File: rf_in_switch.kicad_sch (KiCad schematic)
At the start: 7 parts, among them P17 CONUFL001-SMD-T, P18 CONUFL001-SMD-T, U31 QPC1022TR7, U32 QPC1022TR7

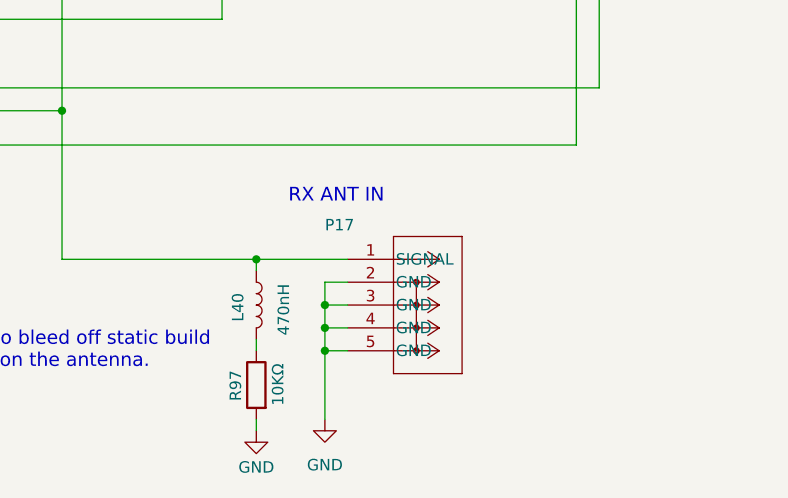
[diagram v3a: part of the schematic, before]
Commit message: Clean up the U.FL connectors a little more
Re-add the ones for TX/RX so both MMCX and U.FL are available.

Move P8 to a better location.

Signed-off-by: Corey Minyard <corey@minyard.net>
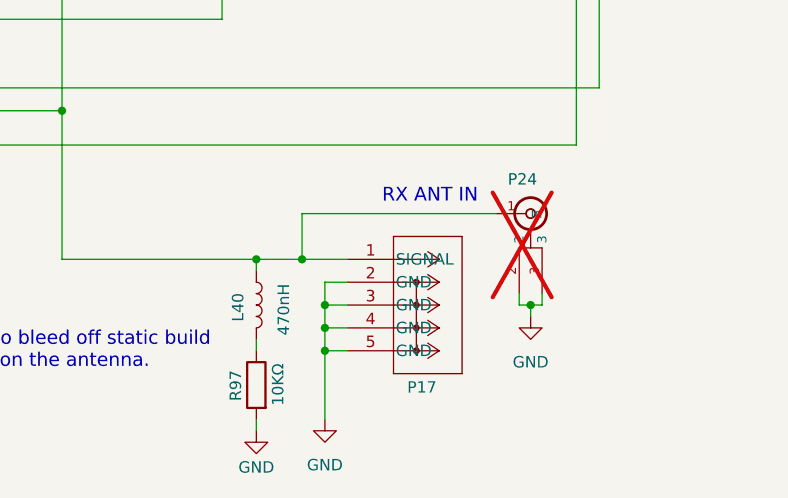
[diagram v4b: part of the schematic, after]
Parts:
- added P24: CONUFL001-SMD-T, PacSatDev_misc:CONN1_CONUFL_TEC, symbol PACSAT_DEV_misc:U_FL
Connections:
- net GND: now also P24.2, P24.3
- net at L40.1, P17.1 (SIGNAL), R96.1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: now also P24.1 (In)
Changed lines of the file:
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@@
 	(text "RX ANT IN"
 		(exclude_from_sim no)
-		(at 157.734 141.224 0)
+		(at 168.148 141.224 0)
 		(effects
 			(font
@@
 	)
 	(junction
+		(at 148.59 147.32)
+		(diameter 0)
+		(color 0 0 0 0)
+	)
+	(junction
 		(at 139.7 113.03)
 		(diameter 0)
@@
 	)
 	(junction
+		(at 173.99 152.4)
+		(diameter 0)
+		(color 0 0 0 0)
+	)
+	(junction
 		(at 151.13 157.48)
 		(diameter 0)
@@
 	(wire
 		(pts
+			(xy 172.72 151.13) (xy 172.72 152.4)
+		)
+		(stroke
+			(width 0)
+			(type default)
+		)
+	)
+	(wire
+		(pts
 			(xy 181.61 109.22) (xy 181.61 128.27)
 		)
@@
 	(wire
 		(pts
+			(xy 148.59 147.32) (xy 153.67 147.32)
+		)
+		(stroke
+			(width 0)
+			(type default)
+		)
+	)
+	(wire
+		(pts
 			(xy 121.92 147.32) (xy 121.92 130.81)
 		)
@@
 	(wire
 		(pts
+			(xy 173.99 152.4) (xy 172.72 152.4)
+		)
+		(stroke
+			(width 0)
+			(type default)
+		)
+	)
+	(wire
+		(pts
 			(xy 104.14 74.93) (xy 109.22 74.93)
 		)
@@
 	(wire
 		(pts
-			(xy 143.51 147.32) (xy 153.67 147.32)
+			(xy 175.26 152.4) (xy 173.99 152.4)
+		)
+		(stroke
+			(width 0)
+			(type default)
+		)
+	)
+	(wire
+		(pts
+			(xy 143.51 147.32) (xy 148.59 147.32)
 		)
 		(stroke
@@
 	(wire
 		(pts
+			(xy 148.59 142.24) (xy 148.59 147.32)
+		)
+		(stroke
+			(width 0)
+			(type default)
+		)
+	)
+	(wire
+		(pts
 			(xy 106.68 53.34) (xy 106.68 68.58)
 		)
@@
 	(wire
 		(pts
+			(xy 173.99 153.67) (xy 173.99 152.4)
+		)
+		(stroke
+			(width 0)
+			(type default)
+		)
+	)
+	(wire
+		(pts
 			(xy 198.12 64.77) (xy 198.12 82.55)
 		)
@@
 	(wire
 		(pts
+			(xy 170.18 142.24) (xy 148.59 142.24)
+		)
+		(stroke
+			(width 0)
+			(type default)
+		)
+	)
+	(wire
+		(pts
 			(xy 163.83 55.88) (xy 163.83 58.42)
 		)
@@
 		(pts
 			(xy 101.6 77.47) (xy 118.11 77.47)
+		)
+		(stroke
+			(width 0)
+			(type default)
+		)
+	)
+	(wire
+		(pts
+			(xy 175.26 151.13) (xy 175.26 152.4)
 		)
 		(stroke
@@
 	)
 	(symbol
+		(lib_id "power:GND")
+		(at 173.99 153.67 0)
+		(mirror y)
+		(unit 1)
+		(exclude_from_sim no)
+		(in_bom yes)
+		(on_board yes)
+		(dnp no)
+		(fields_autoplaced yes)
+		(property "Reference" "#PWR0253"
+			(at 173.99 160.02 0)
+			(effects
+				(font
+					(size 1.27 1.27)
+				)
+				(hide yes)
+			)
+		)
+		(property "Value" "GND"
+			(at 173.99 158.75 0)
+			(effects
+				(font
+					(size 1.27 1.27)
+				)
+			)
+		)
+		(property "Footprint" ""
+			(at 173.99 153.67 0)
+			(effects
+				(font
+					(size 1.27 1.27)
+				)
+				(hide yes)
+			)
+		)
+		(property "Datasheet" ""
+			(at 173.99 153.67 0)
+			(effects
+				(font
+					(size 1.27 1.27)
+				)
+				(hide yes)
+			)
+		)
+		(property "Description" ""
+			(at 173.99 153.67 0)
+			(effects
+				(font
+					(size 1.27 1.27)
+				)
+			)
+		)
+		(pin "1"
+		)
+		(instances
+			(project "PacSat_AFSK"
+				(path "/cc9f42d2-6985-41ac-acab-5ab7b01c5b38/4fa888af-703c-49ed-93bb-d56d2f02c470/64a91b23-a882-4658-bea9-c6c8274e2ac4"
+					(reference "#PWR0253")
+					(unit 1)
+				)
+			)
+		)
+	)
+	(symbol
 		(lib_id "power:+5V")
 		(at 83.82 118.11 0)
@@
 				(path "/cc9f42d2-6985-41ac-acab-5ab7b01c5b38/4fa888af-703c-49ed-93bb-d56d2f02c470/64a91b23-a882-4658-bea9-c6c8274e2ac4"
 					(reference "#PWR0275")
+					(unit 1)
+				)
+			)
+		)
+	)
+	(symbol
+		(lib_id "PACSAT_DEV_misc:U_FL")
+		(at 173.99 142.24 0)
+		(unit 1)
+		(exclude_from_sim no)
+		(in_bom no)
+		(on_board yes)
+		(dnp yes)
+		(property "Reference" "P24"
+			(at 171.45 138.43 0)
+			(effects
+				(font
+					(size 1.27 1.27)
+				)
+				(justify left)
+			)
+		)
+		(property "Value" "CONUFL001-SMD-T"
+			(at 173.99 142.24 0)
+			(effects
+				(font
+					(size 1.27 1.27)
+				)
+				(hide yes)
+			)
+		)
+		(property "Footprint" "PacSatDev_misc:CONN1_CONUFL_TEC"
+			(at 173.99 142.24 0)
+			(effects
+				(font
+					(size 1.27 1.27)
+				)
+				(hide yes)
+			)
+		)
+		(property "Datasheet" ""
+			(at 173.99 142.24 0)
+			(effects
+				(font
+					(size 1.27 1.27)
+				)
+				(hide yes)
+			)
+		)
+		(property "Description" ""
+			(at 173.99 142.24 0)
+			(effects
+				(font
+					(size 1.27 1.27)
+				)
+			)
+		)
+		(pin "1"
+		)
+		(pin "2"
+		)
+		(pin "3"
+		)
+		(instances
+			(project "PacSat_AFSK"
+				(path "/cc9f42d2-6985-41ac-acab-5ab7b01c5b38/4fa888af-703c-49ed-93bb-d56d2f02c470/64a91b23-a882-4658-bea9-c6c8274e2ac4"
+					(reference "P24")
 					(unit 1)
 				)
@@
 		(dnp no)
 		(property "Reference" "P17"
-			(at 151.13 143.51 0)
-			(effects
-				(font
+			(at 160.274 161.544 0)
+			(effects
+				(font

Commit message: Set the part number right for the MMCX connectors
Signed-off-by: Corey Minyard <corey@minyard.net>
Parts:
- P17: value CONUFL001-SMD-T -> MMCX-J-P-H-ST-TH1
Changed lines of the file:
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@@
 			)
 		)
-		(property "Value" "CONUFL001-SMD-T"
+		(property "Value" "MMCX-J-P-H-ST-TH1"
 			(at 153.67 147.32 0)
 			(effects

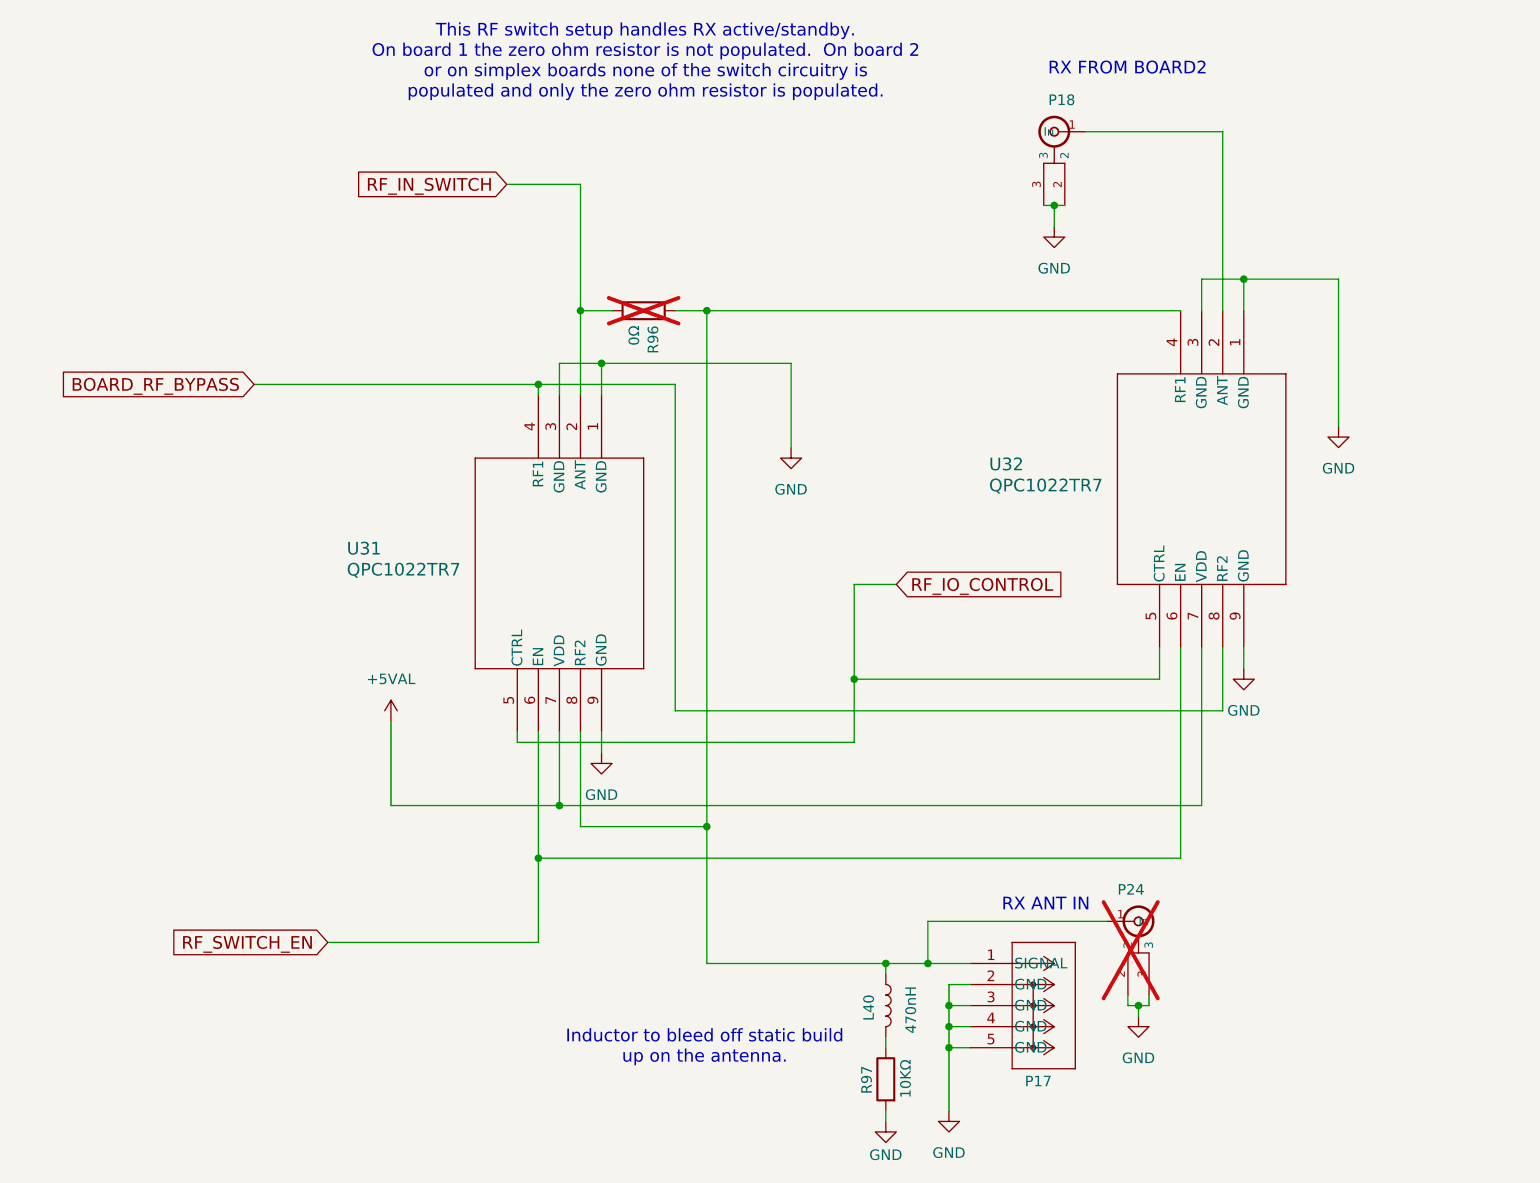
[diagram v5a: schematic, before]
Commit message: Rework RF switches, remove loopback
The loopback just wasn't going to work.  Use a different, more suitable
RF switch.  This required adding a new power converter for 3.3VAL.

Move the power limiters to their own sheet to make things a little more
roomy on the power sheet.

Signed-off-by: Corey Minyard <corey@minyard.net>
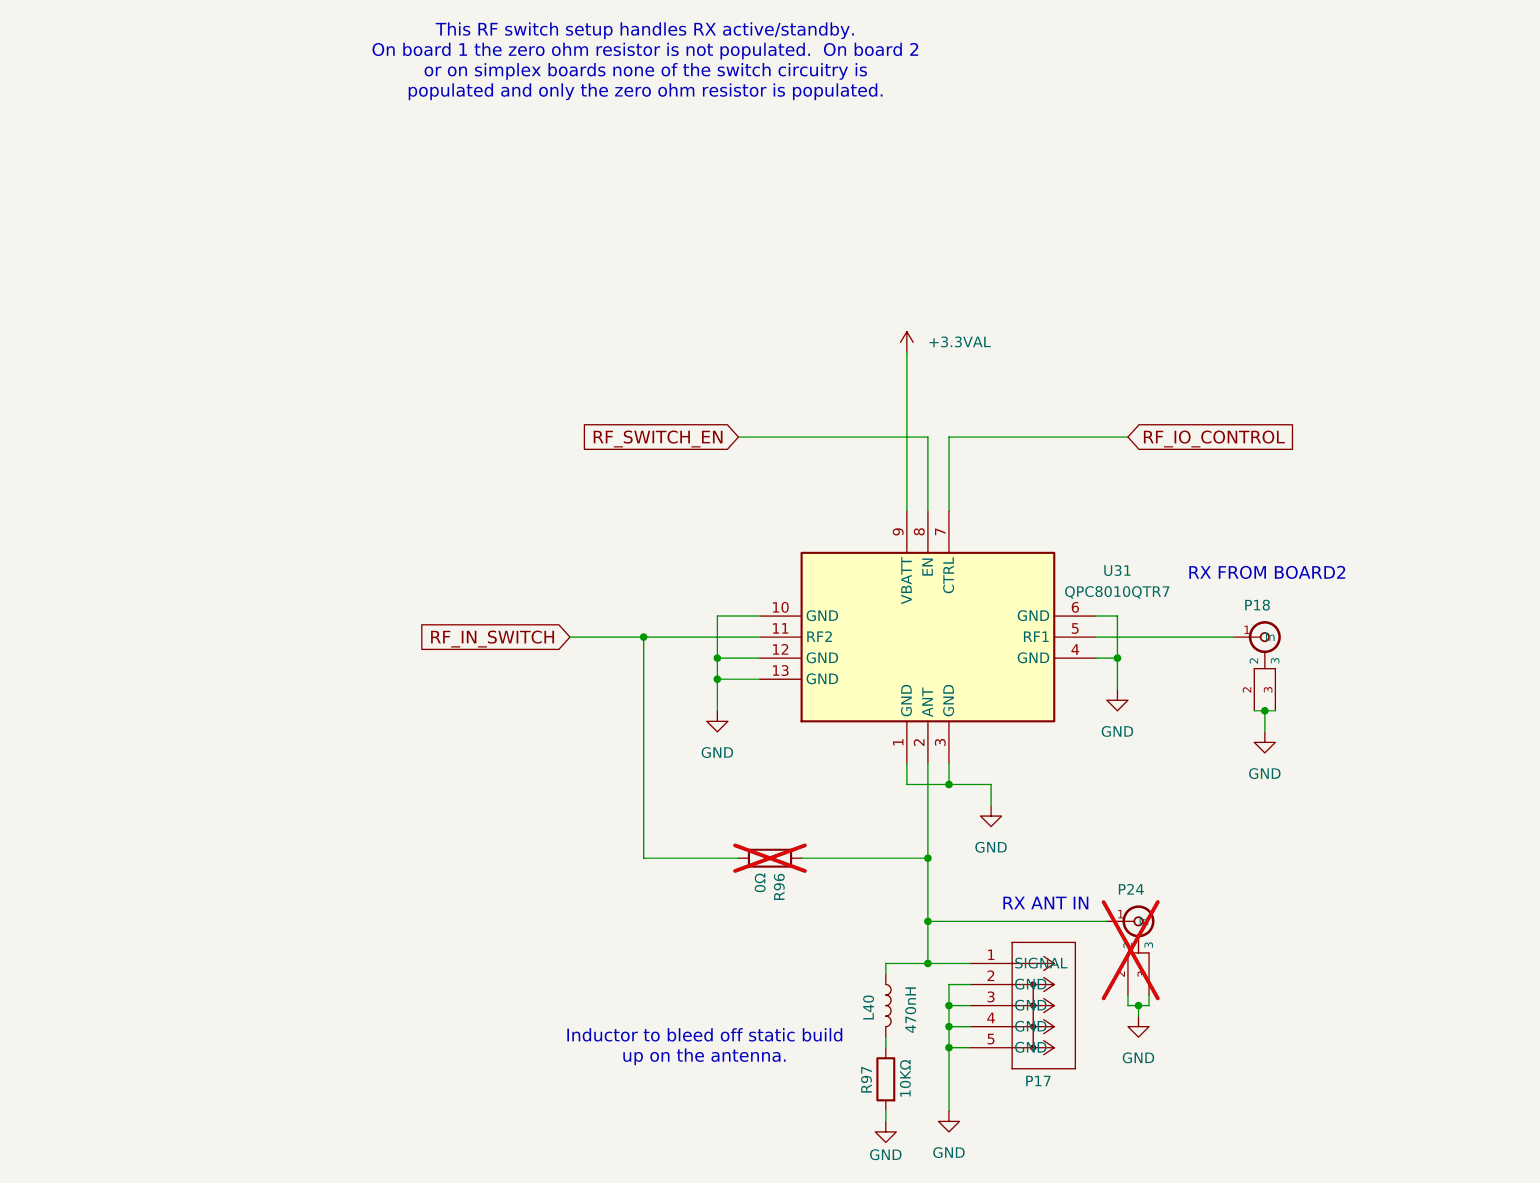
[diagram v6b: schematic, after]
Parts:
- removed U31, U32: QPC1022TR7, PacSatDev_misc:QPC1022_QOR, symbol PACSAT_DEV_misc:QPC1022TR7
- added U31: QPC8010QTR7, PacSatDev_misc:QFN50P200X200X60-13N-D, symbol PACSAT_DEV_misc:QPC8010QTR7
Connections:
- net GND: now also U31.1 (GND), U31.10 (GND), U31.12 (GND), U31.13 (GND), U31.3 (GND), U31.4 (GND), U31.6 (GND)
- net RF_IN_SWITCH: now also U31.11 (RF2)
- net RF_IO_CONTROL: now also U31.7 (CTRL)
- net RF_SWITCH_EN: now also U31.8 (EN)
- net at L40.1, P17.1 (SIGNAL), P24.1 (In)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: now also U31.2 (ANT)
- net at P18.1 (In): now also U31.5 (RF1)
- new net +3.3VAL: U31.9 (VBATT)
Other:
- moved on the sheet: P18, R96

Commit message: Fixes for the RF switch changes
The RF outputs were backwards and needed to be switched.  That required
flipping the chips to the top and the bypass resistors to the bottom.

Fix various documentation around the new parts and the loss of the
loopback function.

Signed-off-by: Corey Minyard <corey@minyard.net>
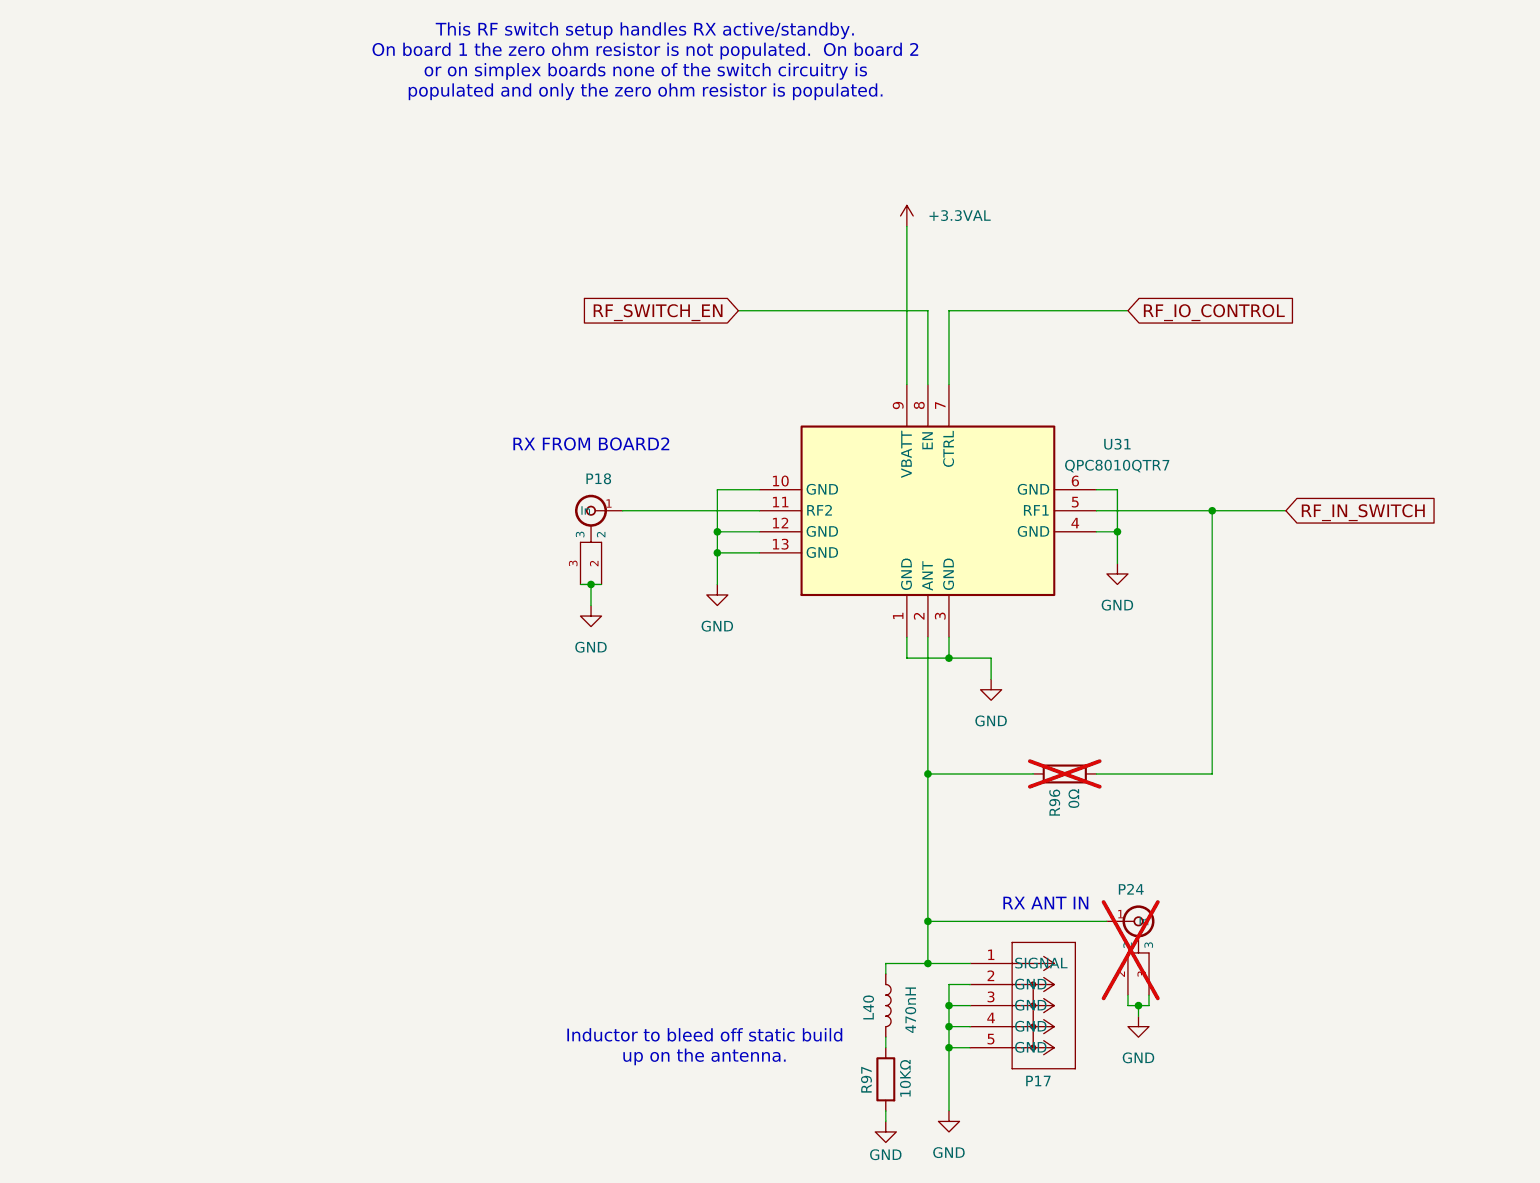
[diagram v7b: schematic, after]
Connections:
- net RF_IN_SWITCH: now also U31.5 (RF1); no longer U31.11 (RF2)
- net at P18.1 (In): now also U31.11 (RF2); no longer U31.5 (RF1)
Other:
- moved on the sheet: P18, R96, U31

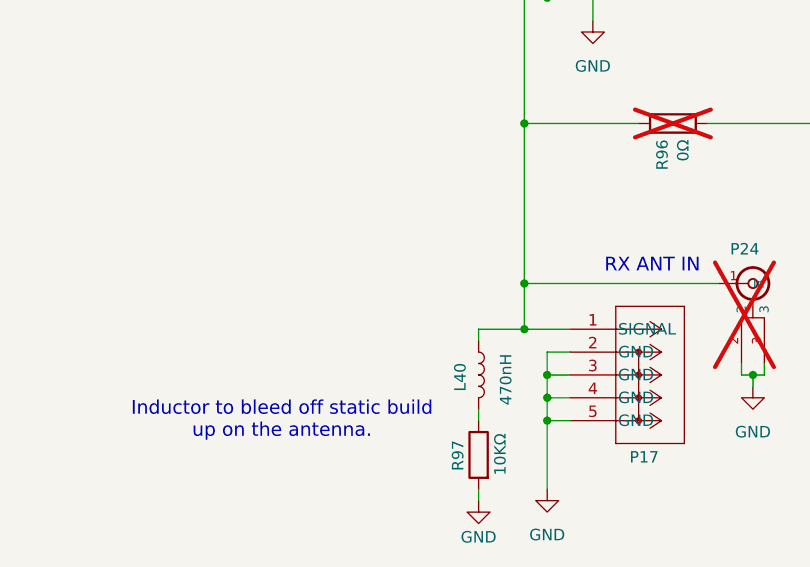
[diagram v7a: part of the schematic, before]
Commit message: Add an optional diplexed antenna input
Signed-off-by: Corey Minyard <corey@minyard.net>
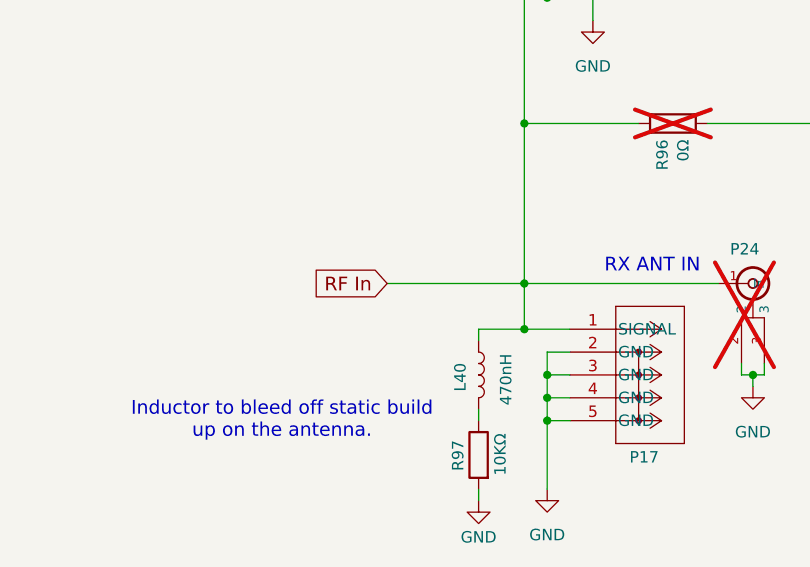
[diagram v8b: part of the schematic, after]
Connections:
- net RF In: now reaches L40.1, P17.1 (SIGNAL), P24.1 (In), R96.1, U31.2 (ANT)
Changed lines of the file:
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@@
+	(wire
+		(pts
+			(xy 133.35 142.24) (xy 148.59 142.24)
+		)
+		(stroke
+			(width 0)
+			(type default)
+		)
+	)
 	(wire
 		(pts
@@
 				(hide yes)
 			)
+		)
+	)
+	(global_label "RF In"
+		(shape input)
+		(at 133.35 142.24 180)
+		(fields_autoplaced yes)
+		(effects
+			(font
+				(size 1.524 1.524)
+			)
+			(justify right)
+		)
+		(property "Intersheetrefs" "${INTERSHEET_REFS}"
+			(at 124.4572 142.24 0)
+			(effects
+				(font
+					(size 1.27 1.27)
+				)
+				(justify right)
+				(hide yes)
+			)
